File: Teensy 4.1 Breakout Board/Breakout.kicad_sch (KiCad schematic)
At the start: 52 parts, among them J1 CAN, J10 RTD_Speaker, J12 RTD_button, J2 12V Power, J3 APPS1, J4 APPS2, J5 Brake_Pressure_Front, J6 Brake_Pressure_Rear, J7 Nextion, J8 ESP32, J9 Brake_Light, Q1 2N7000, Q2 2N7000, U1 SN65HVD230, U3 Teensy4.1, U4 TPS62163DSG, U5 MPU6050

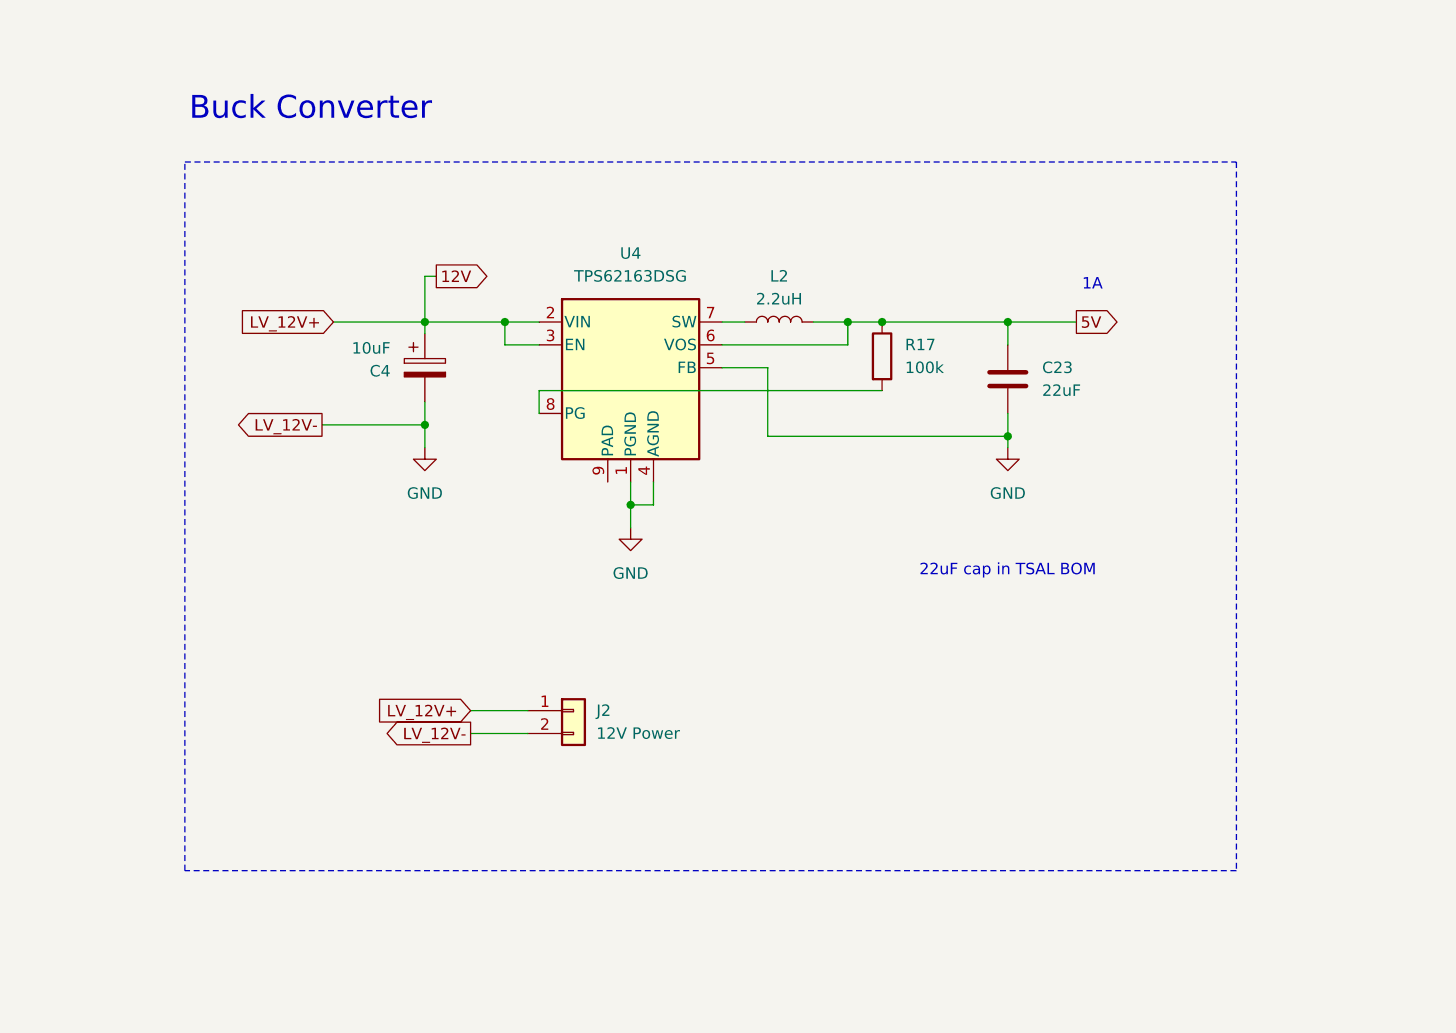
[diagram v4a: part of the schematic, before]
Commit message: updated breakout
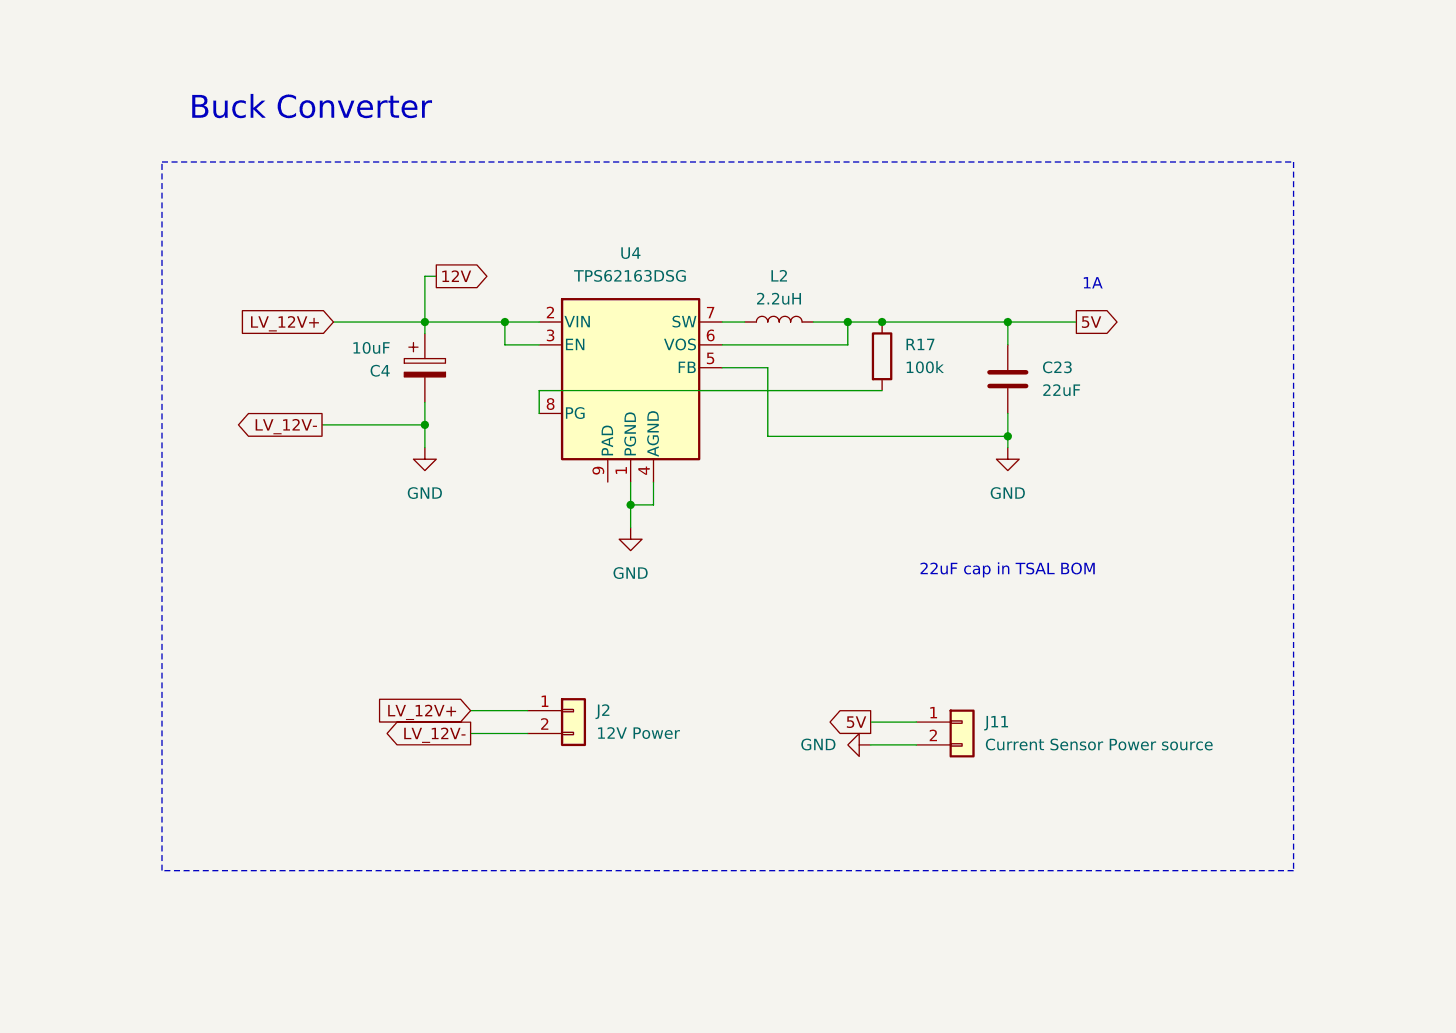
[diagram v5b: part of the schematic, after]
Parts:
- added J11: Current Sensor Power source, Connector_JST:JST_XH_B2B-XH-A_1x02_P2.50mm_Vertical, symbol Connector_Generic:Conn_01x02
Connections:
- net 5V: now also J11.1 (Pin_1)
- net GND: now also J11.2 (Pin_2)
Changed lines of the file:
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@@
 	)
 	(rectangle
-		(start 76.2 273.05)
-		(end 193.04 351.79)
+		(start 73.66 273.05)
+		(end 199.39 351.79)
 		(stroke
 			(width 0)
@@
 	(wire
 		(pts
+			(xy 152.4 335.28) (xy 157.48 335.28)
+		)
+		(stroke
+			(width 0)
+			(type default)
+		)
+	)
+	(wire
+		(pts
 			(xy 270.51 215.9) (xy 276.86 215.9)
 		)
@@
 	(wire
 		(pts
+			(xy 152.4 337.82) (xy 157.48 337.82)
+		)
+		(stroke
+			(width 0)
+			(type default)
+		)
+	)
+	(wire
+		(pts
 			(xy 381 327.66) (xy 381 330.2)
 		)
@@
 		)
 	)
+	(global_label "5V"
+		(shape output)
+		(at 152.4 335.28 180)
+		(effects
+			(font
+				(size 1.27 1.27)
+			)
+			(justify right)
+		)
+		(property "Intersheetrefs" "${INTERSHEET_REFS}"
+			(at 146.1648 335.2006 0)
+			(effects
+				(font
+					(size 1.27 1.27)
+				)
+				(justify right)
+				(hide yes)
+			)
+		)
+	)
 	(global_label "LV_12V-"
 		(shape output)
@@
 	)
 	(symbol
+		(lib_id "Connector_Generic:Conn_01x02")
+		(at 162.56 335.28 0)
+		(unit 1)
+		(exclude_from_sim no)
+		(in_bom yes)
+		(on_board yes)
+		(dnp no)
+		(fields_autoplaced yes)
+		(property "Reference" "J11"
+			(at 165.1 335.2799 0)
+			(effects
+				(font
+					(size 1.27 1.27)
+				)
+				(justify left)
+			)
+		)
+		(property "Value" "Current Sensor Power source"
+			(at 165.1 337.8199 0)
+			(effects
+				(font
+					(size 1.27 1.27)
+				)
+				(justify left)
+			)
+		)
+		(property "Footprint" "Connector_JST:JST_XH_B2B-XH-A_1x02_P2.50mm_Vertical"
+			(at 162.56 335.28 0)
+			(effects
+				(font
+					(size 1.27 1.27)
+				)
+				(hide yes)
+			)
+		)
+		(property "Datasheet" "https://www.jst-mfg.com/product/pdf/eng/eXH.pdf"
+			(at 162.56 335.28 0)
+			(effects
+				(font
+					(size 1.27 1.27)
+				)
+				(hide yes)
+			)
+		)
+		(property "Description" "Generic connector, single row, 01x02, script generated (kicad-library-utils/schlib/autogen/connector/)"
+			(at 162.56 335.28 0)
+			(effects
+				(font
+					(size 1.27 1.27)
+				)
+				(hide yes)
+			)
+		)
+		(property "Sim.Device" ""
+			(at 162.56 335.28 0)
+			(effects
+				(font
+					(size 1.27 1.27)
+				)
+				(hide yes)
+			)
+		)
+		(property "Sim.Pins" ""
+			(at 162.56 335.28 0)
+			(effects
+				(font
+					(size 1.27 1.27)
+				)
+				(hide yes)
+			)
+		)
+		(property "Sim.Type" ""
+			(at 162.56 335.28 0)
+			(effects
+				(font
+					(size 1.27 1.27)
+				)
+				(hide yes)
+			)
+		)
+		(property "Part Number" "B2B-XH-A"
+			(at 162.56 335.28 0)
+			(effects
+				(font
+					(size 1.27 1.27)
+				)
+				(hide yes)
+			)
+		)
+		(pin "2"
+		)
+		(pin "1"
+		)
+		(instances
+			(project "Breakout"
+				(path "/d093329e-1533-4bb2-af31-8d89d9afb117"
+					(reference "J11")
+					(unit 1)
+				)
+			)
+		)
+	)
+	(symbol
 		(lib_id "Device:C")
 		(at 365.76 297.18 0)
@@
 					(unit 1)
 				)
+			)
+		)
+	)
+	(symbol
+		(lib_id "power:GND")
+		(at 152.4 337.82 270)
+		(unit 1)
+		(exclude_from_sim no)
+		(in_bom yes)
+		(on_board yes)
+		(dnp no)
+		(fields_autoplaced yes)
+		(property "Reference" "#PWR031"
+			(at 146.05 337.82 0)
+			(effects
+				(font
+					(size 1.27 1.27)
+				)
+				(hide yes)
+			)
+		)
+		(property "Value" "GND"
+			(at 148.59 337.8199 90)
+			(effects
+				(font
+					(size 1.27 1.27)
+				)
+				(justify right)
+			)
+		)
+		(property "Footprint" ""
+			(at 152.4 337.82 0)
+			(effects
+				(font
+					(size 1.27 1.27)
+				)
+				(hide yes)
+			)
+		)
+		(property "Datasheet" ""
+			(at 152.4 337.82 0)
+			(effects
+				(font
+					(size 1.27 1.27)
+				)
+				(hide yes)
+			)
+		)
+		(property "Description" "Power symbol creates a global label with name \"GND\" , ground"
+			(at 152.4 337.82 0)
+			(effects
+				(font
+					(size 1.27 1.27)
+				)
+				(hide yes)
+			)
+		)
+		(pin "1"
+		)
+		(instances
+			(project "Breakout"
+				(path "/d093329e-1533-4bb2-af31-8d89d9afb117"
+					(reference "#PWR031")
+					(unit 1)
+				)

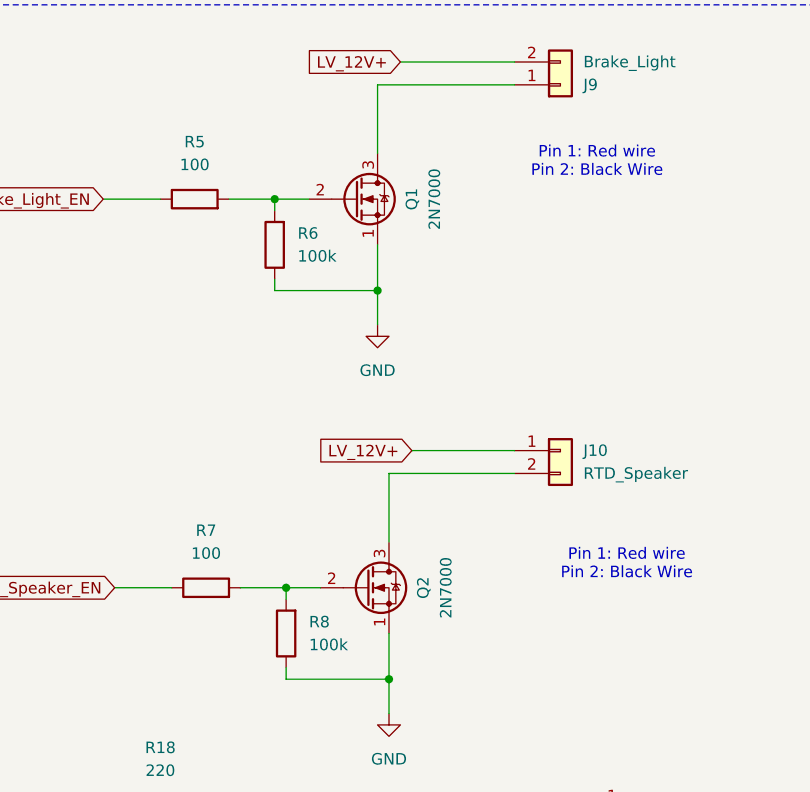
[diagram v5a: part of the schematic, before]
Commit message: slave with new fuses added
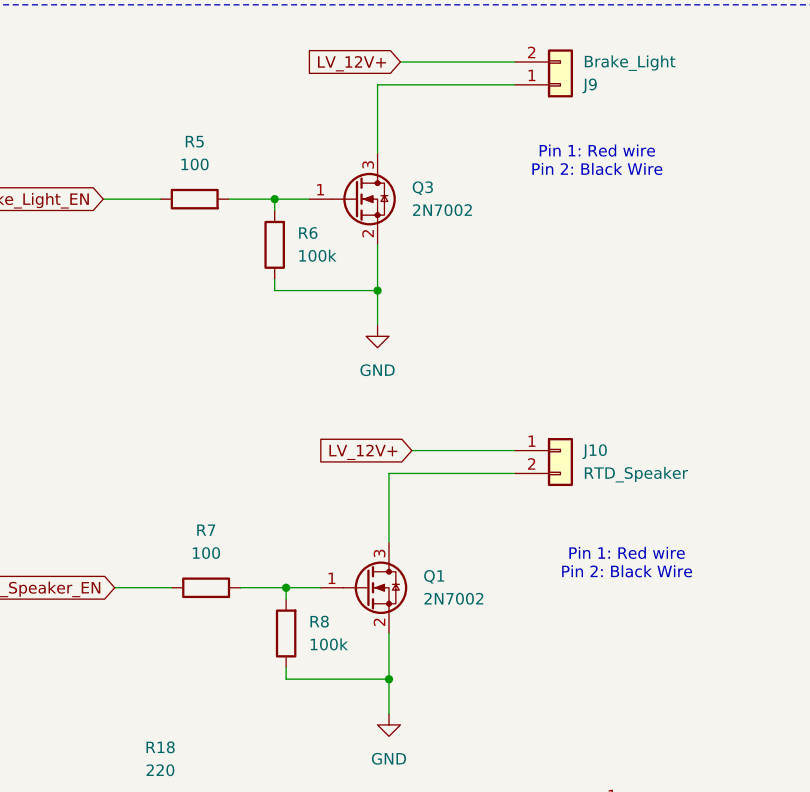
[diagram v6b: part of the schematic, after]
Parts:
- removed Q1, Q2: 2N7000, Package_TO_SOT_THT:TO-92_Inline, symbol Transistor_FET:2N7000
- added Q1, Q3: 2N7002, Package_TO_SOT_SMD:SOT-23, symbol Transistor_FET:2N7002
- L2: Part Number (none) -> XFL3012-222MEC
- R17: Part Number MCF 0.25W 100k -> MCF 0.25W 100K
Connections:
- net GND: now also Q1.2 (S), Q3.2 (S)
- net at R5.2, R6.2: now also Q3.1 (G)
- net at R7.2, R8.2: now also Q1.1 (G)
- net at J9.1 (Pin_1): now also Q3.3 (D)
- net at J10.2 (Pin_2): now also Q1.3 (D)
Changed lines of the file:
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@@
 			)
 		)
-		(property "Part Number" "MCF 0.25W 100k"
+		(property "Part Number" "MCF 0.25W 100K"
 			(at 153.67 294.64 0)
 			(effects
@@
 	)
 	(symbol
+		(lib_id "Transistor_FET:2N7002")
+		(at 270.51 289.56 0)
+		(unit 1)
+		(exclude_from_sim no)
+		(in_bom yes)
+		(on_board yes)
+		(dnp no)
+		(fields_autoplaced yes)
+		(property "Reference" "Q3"
+			(at 276.86 288.2899 0)
+			(effects
+				(font
+					(size 1.27 1.27)
+				)
+				(justify left)
+			)
+		)
+		(property "Value" "2N7002"
+			(at 276.86 290.8299 0)
+			(effects
+				(font
+					(size 1.27 1.27)
+				)
+				(justify left)
+			)
+		)
+		(property "Footprint" "Package_TO_SOT_SMD:SOT-23"
+			(at 275.59 291.465 0)
+			(effects
+				(font
+					(size 1.27 1.27)
+					(italic yes)
+				)
+				(justify left)
+				(hide yes)
+			)
+		)
+		(property "Datasheet" "https://www.onsemi.com/pub/Collateral/NDS7002A-D.PDF"
+			(at 275.59 293.37 0)
+			(effects
+				(font
+					(size 1.27 1.27)
+				)
+				(justify left)
+				(hide yes)
+			)
+		)
+		(property "Description" "0.115A Id, 60V Vds, N-Channel MOSFET, SOT-23"
+			(at 270.51 289.56 0)
+			(effects
+				(font
+					(size 1.27 1.27)
+				)
+				(hide yes)
+			)
+		)
+		(pin "2"
+		)
+		(pin "3"
+		)
+		(pin "1"
+		)
+		(instances
+			(project ""
+				(path "/d093329e-1533-4bb2-af31-8d89d9afb117"
+					(reference "Q3")
+					(unit 1)
+				)
+			)
+		)
+	)
+	(symbol
 		(lib_id "Device:R")
 		(at 383.54 297.18 0)
@@
 			)
 		)
+		(property "Part Number" "XFL3012-222MEC"
+			(at 142.24 290.83 90)
+			(effects
+				(font
+					(size 1.27 1.27)
+				)
+				(hide yes)
+			)
+		)
 		(pin "2"
 		)
@@
 			)
 		)
-		(property "Description" "Adafruit MPU6050"
+		(property "Description" ""
 			(at 287.02 213.36 0)
 			(effects
@@
 	)
 	(symbol
-		(lib_id "Transistor_FET:2N7000")
-		(at 270.51 289.56 0)
-		(unit 1)
-		(exclude_from_sim no)
-		(in_bom yes)
-		(on_board yes)
-		(dnp no)
-		(property "Reference" "Q1"
-			(at 276.86 289.56 90)
-			(effects
-				(font
-					(size 1.27 1.27)
-				)
-			)
-		)
-		(property "Value" "2N7000"
-			(at 279.4 289.56 90)
-			(effects
-				(font
-					(size 1.27 1.27)
-				)
-			)
-		)
-		(property "Footprint" "Package_TO_SOT_THT:TO-92_Inline"
-			(at 275.59 291.465 0)
-			(effects
-				(font
-					(size 1.27 1.27)
-					(italic yes)
-				)
-				(justify left)
-				(hide yes)
-			)
-		)
-		(property "Datasheet" "https://www.onsemi.com/download/data-sheet/pdf/nds7002a-d.pdf"
-			(at 275.59 293.37 0)
-			(effects
-				(font
-					(size 1.27 1.27)
-				)
-				(justify left)
-				(hide yes)
-			)
-		)
-		(property "Description" "0.2A Id, 200V Vds, N-Channel MOSFET, 2.6V Logic Level, TO-92"
-			(at 270.51 289.56 0)
-			(effects
-				(font
-					(size 1.27 1.27)
-				)
-				(hide yes)
-			)
-		)
-		(property "Part Number" "2N7000"
-			(at 270.51 289.56 0)
-			(effects
-				(font
-					(size 1.27 1.27)
-				)
-				(hide yes)
-			)
-		)
-		(property "Sim.Device" ""
-			(at 270.51 289.56 90)
-			(effects
-				(font
-					(size 1.27 1.27)
-				)
-				(hide yes)
-			)
-		)
-		(property "Sim.Pins" ""
-			(at 270.51 289.56 90)
-			(effects
-				(font
-					(size 1.27 1.27)
-				)
-				(hide yes)
-			)
-		)
-		(property "Sim.Type" ""
-			(at 270.51 289.56 90)
-			(effects
-				(font
-					(size 1.27 1.27)
-				)
-				(hide yes)
-			)
-		)
-		(pin "2"
-		)
-		(pin "3"
-		)
-		(pin "1"
-		)
-		(instances
-			(project "Breakout"
-				(path "/d093329e-1533-4bb2-af31-8d89d9afb117"
-					(reference "Q1")
-					(unit 1)
-				)
-			)
-		)
-	)
-	(symbol
 		(lib_id "Connector_Generic:Conn_01x03")
 		(at 483.87 285.75 0)
@@
 	)
 	(symbol
-		(lib_id "Transistor_FET:2N7000")
-		(at 271.78 332.74 0)
-		(unit 1)
-		(exclude_from_sim no)
-		(in_bom yes)
-		(on_board yes)
-		(dnp no)
-		(property "Reference" "Q2"
-			(at 278.13 332.74 90)
-			(effects
-				(font
-					(size 1.27 1.27)
-				)
-			)
-		)
-		(property "Value" "2N7000"
-			(at 280.67 332.74 90)
-			(effects
-				(font
-					(size 1.27 1.27)
-				)
-			)
-		)
-		(property "Footprint" "Package_TO_SOT_THT:TO-92_Inline"
-			(at 276.86 334.645 0)
-			(effects
-				(font
-					(size 1.27 1.27)
-					(italic yes)
-				)
-				(justify left)
-				(hide yes)
-			)
-		)
-		(property "Datasheet" "https://www.onsemi.com/download/data-sheet/pdf/nds7002a-d.pdf"
-			(at 276.86 336.55 0)
-			(effects
-				(font
-					(size 1.27 1.27)
-				)
-				(justify left)
-				(hide yes)
-			)
-		)
-		(property "Description" "0.2A Id, 200V Vds, N-Channel MOSFET, 2.6V Logic Level, TO-92"
-			(at 271.78 332.74 0)
-			(effects
-				(font
-					(size 1.27 1.27)
-				)
-				(hide yes)
-			)
-		)
-		(property "Part Number" "2N7000"
-			(at 271.78 332.74 0)
-			(effects
-				(font
-					(size 1.27 1.27)
-				)
-				(hide yes)
-			)
-		)
-		(property "Sim.Device" ""
-			(at 271.78 332.74 90)
-			(effects
-				(font
-					(size 1.27 1.27)
-				)
-				(hide yes)
-			)
-		)
-		(property "Sim.Pins" ""
-			(at 271.78 332.74 90)
-			(effects
-				(font
-					(size 1.27 1.27)
-				)
-				(hide yes)
-			)
-		)
-		(property "Sim.Type" ""
-			(at 271.78 332.74 90)
-			(effects
-				(font
-					(size 1.27 1.27)
-				)
-				(hide yes)
-			)
-		)
-		(pin "2"
-		)
-		(pin "3"
-		)
-		(pin "1"
-		)
-		(instances
-			(project "Breakout"
-				(path "/d093329e-1533-4bb2-af31-8d89d9afb117"
-					(reference "Q2")
-					(unit 1)
-				)
-			)
-		)
-	)
-	(symbol
 		(lib_id "Device:C")
 		(at 381 157.48 0)
@@
 					(unit 1)
 				)
+			)
+		)
+	)
+	(symbol
+		(lib_id "Transistor_FET:2N7002")
+		(at 271.78 332.74 0)
+		(unit 1)
+		(exclude_from_sim no)
+		(in_bom yes)
+		(on_board yes)
+		(dnp no)
+		(fields_autoplaced yes)
+		(property "Reference" "Q1"
+			(at 278.13 331.4699 0)
+			(effects
+				(font
+					(size 1.27 1.27)
+				)
+				(justify left)
+			)
+		)
+		(property "Value" "2N7002"
+			(at 278.13 334.0099 0)
+			(effects
+				(font
+					(size 1.27 1.27)
+				)
+				(justify left)
+			)
+		)
+		(property "Footprint" "Package_TO_SOT_SMD:SOT-23"
+			(at 276.86 334.645 0)
+			(effects
+				(font
+					(size 1.27 1.27)
+					(italic yes)
+				)
+				(justify left)
+				(hide yes)
+			)
+		)
+		(property "Datasheet" "https://www.onsemi.com/pub/Collateral/NDS7002A-D.PDF"
+			(at 276.86 336.55 0)
+			(effects
+				(font
+					(size 1.27 1.27)
+				)
+				(justify left)
+				(hide yes)
+			)
+		)
+		(property "Description" "0.115A Id, 60V Vds, N-Channel MOSFET, SOT-23"
+			(at 271.78 332.74 0)
+			(effects
+				(font
+					(size 1.27 1.27)
+				)
+				(hide yes)
+			)
+		)
+		(pin "2"
+		)
+		(pin "3"
+		)
+		(pin "1"
+		)
+		(instances
+			(project "Breakout"
+				(path "/d093329e-1533-4bb2-af31-8d89d9afb117"
+					(reference "Q1")
+					(unit 1)
+				)

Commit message: copied teensy and apps schematic for esf screenshot
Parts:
- removed Q1, Q3: 2N7002, Package_TO_SOT_SMD:SOT-23, symbol Transistor_FET:2N7002
- added C11: 0.1uF, FA14_Capacitor:FA18X7R1H104KNU00, symbol Device:C
- added C12: 10uF, Capacitor_THT:CP_Radial_D5.0mm_P2.50mm, symbol Device:C_Polarized
- added Q1, Q2: 2N7000, Package_TO_SOT_THT:TO-92_Inline, symbol Transistor_FET:2N7000
- added U2: Teensy4.1, teensy.pretty-master:Teensy41, symbol teensy:Teensy4.1
- L2: Part Number XFL3012-222MEC -> (none)
- R17: Part Number MCF 0.25W 100K -> MCF 0.25W 100k
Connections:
- net 3.3V: now also U2.46 (3V3); no longer U3.46 (3V3)
- net 5V: now also C11.2, C12.1, U2.48 (VIN)
- net APPS1_3.3V: now also U2.36 (14_A0_TX3_SPDIF_OUT)
- net APPS2_3.3V: now also U2.37 (15_A1_RX3_SPDIF_IN)
- net Brake_Front_3.3V: now also U2.38 (16_A2_RX4_SCL1); no longer U3.38 (16_A2_RX4_SCL1)
- net Brake_Light_EN: now also U2.8 (6_OUT1D); no longer U3.8 (6_OUT1D)
- net Brake_Rear_3.3V: now also U2.39 (17_A3_TX4_SDA1); no longer U3.39 (17_A3_TX4_SDA1)
- net CAN1_RX: now also U2.45 (23_A9_CRX1_MCLK1); no longer U3.45 (23_A9_CRX1_MCLK1)
- net CAN1_TX: now also U2.44 (22_A8_CTX1); no longer U3.44 (22_A8_CTX1)
- net ESP32_RX: now also U2.10 (8_TX2_IN1); no longer U3.10 (8_TX2_IN1)
- net ESP32_TX: now also U2.9 (7_RX2_OUT1A); no longer U3.9 (7_RX2_OUT1A)
- net GND: now also C11.1, C12.2, Q1.1 (S), Q2.1 (S), U2.47 (GND)
- net MPU_SCL: now also U2.41 (19_A5_SCL); no longer U3.41 (19_A5_SCL)
- net MPU_SDA: now also U2.40 (18_A4_SDA); no longer U3.40 (18_A4_SDA)
- net Nextion_RX: now also U2.3 (1_TX1_CTX2_MISO1); no longer U3.3 (1_TX1_CTX2_MISO1)
- net Nextion_TX: now also U2.2 (0_RX1_CRX2_CS1); no longer U3.2 (0_RX1_CRX2_CS1)
- net Precharge_EN: now also U2.5 (3_LRCLK2); no longer U3.5 (3_LRCLK2)
- net RTD_Speaker_EN: now also U2.11 (9_OUT1C); no longer U3.11 (9_OUT1C)
- net RTD_button: now also U2.4 (2_OUT2); no longer U3.4 (2_OUT2)
- net at R5.2, R6.2: now also Q1.2 (G)
- net at R7.2, R8.2: now also Q2.2 (G)
- net at J9.1 (Pin_1): now also Q1.3 (D)
- net at J10.2 (Pin_2): now also Q2.3 (D)
- no-connect marks 2 -> 3
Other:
- note added: "APPS Sensors"
- note removed: "Analogue Sensors"
- note removed: "LP Filter should be physically close to Teensy"
- moved on the sheet: C10, C23, C3, C4, C5, C6, C7, C8, C9, J10, J11, J12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
